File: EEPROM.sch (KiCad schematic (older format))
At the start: 7 parts, among them IC1 M24M02-DRMN6TP

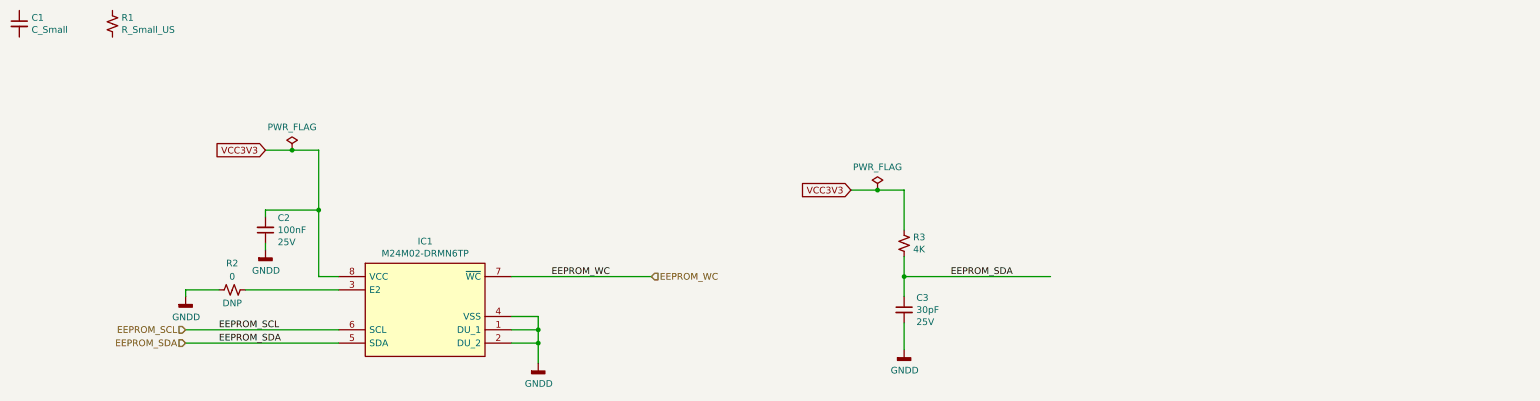
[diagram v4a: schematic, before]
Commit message: Completed FPGA power sheet completed USB3 completed FPGA config
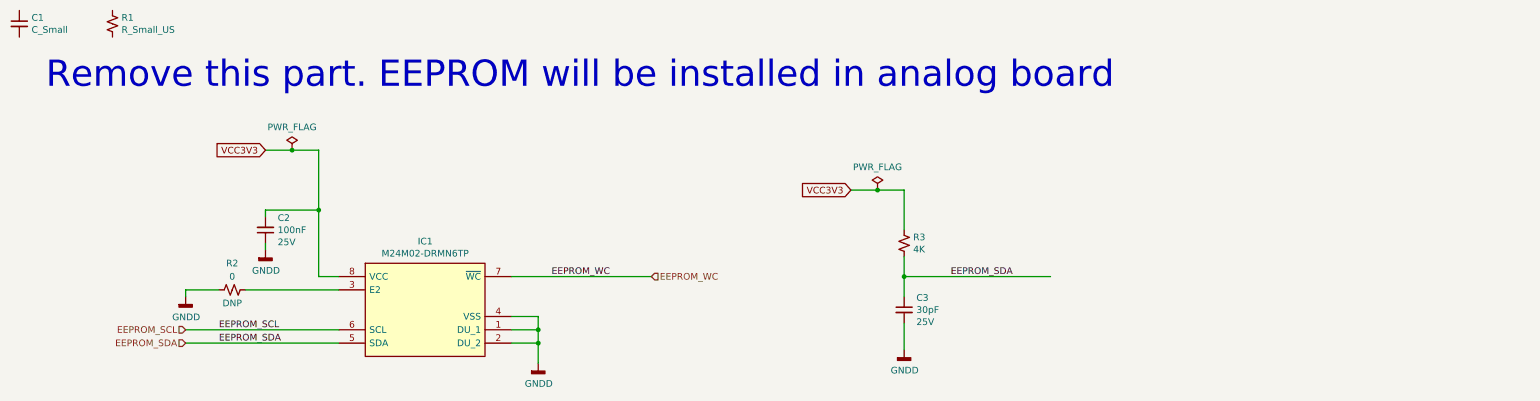
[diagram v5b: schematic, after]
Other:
- note added: "Remove this part. EEPROM will be installed in analog board"
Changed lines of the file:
@@
 	1    0    0    -1
 $EndComp
+Text Notes 1450 2000 0    197  ~ 0
+Remove this part. EEPROM will be installed in analog board
 $EndSCHEMATC

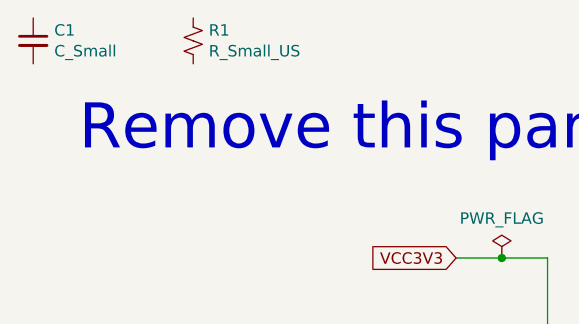
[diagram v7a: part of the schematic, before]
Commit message: Added bus lines -ETH_PHY_CONN -RAM -USB2 Made Output the port direction of clkout of Clock_Gen Placed sheet entris of sheet symbols on top sheet
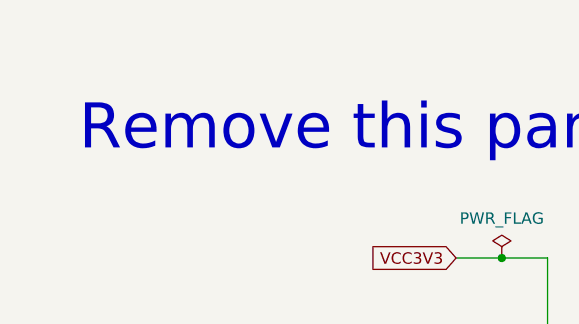
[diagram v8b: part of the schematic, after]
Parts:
- removed C1: C_Small, Capacitor_SMD:C_0603_1608Metric_Pad1.08x0.95mm_HandSolder, symbol Device:C_Small
- removed R1: R_Small_US, Resistor_SMD:R_0603_1608Metric_Pad0.98x0.95mm_HandSolder, symbol Device:R_Small_US
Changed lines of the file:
@@
 $Descr A4 11693 8268
 encoding utf-8
-Sheet 9 19
+Sheet 7 20
 Title "CGMPCX1006"
 Date "2021-02-03"
@@
 Wire Wire Line
 	7900 2750 7900 3050
-$Comp
-L Device:R_Small_US R1
-U 1 1 601D9F52
-P 1950 1500
-F 0 "R1" H 2018 1546 50  0000 L CNN
-F 1 "R_Small_US" H 2018 1455 50  0000 L CNN
-F 2 "Resistor_SMD:R_0603_1608Metric_Pad0.98x0.95mm_HandSolder" H 1950 1500 50  0001 C CNN
-F 3 "~" H 1950 1500 50  0001 C CNN
-	1    1950 1500
-	1    0    0    -1
-$EndComp
-$Comp
-L Device:C_Small C1
-U 1 1 601D8FE6
-P 1250 1500
-F 0 "C1" H 1342 1546 50  0000 L CNN
-F 1 "C_Small" H 1342 1455 50  0000 L CNN
-F 2 "Capacitor_SMD:C_0603_1608Metric_Pad1.08x0.95mm_HandSolder" H 1250 1500 50  0001 C CNN
-F 3 "~" H 1250 1500 50  0001 C CNN
-F 4 "" H 1250 1500 50  0000 C CNN "Voltage"
-	1    1250 1500
-	1    0    0    -1
-$EndComp
 Text Notes 1450 2000 0    197  ~ 0
 Remove this part. EEPROM will be installed in analog board
